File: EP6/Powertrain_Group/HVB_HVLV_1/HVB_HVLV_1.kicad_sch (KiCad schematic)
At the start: 20 parts, among them J1 HV+, J2 HV-, J3 from LV, J5 DCDC-, J6 DCDC+, K1 G7L-2A-X DC24, K2 DBT72410, Q1 IXTH6N100D2, U1 PC817

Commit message: update HVB_HVLV_1 V2.1
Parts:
- removed K1: G7L-2A-X DC24, nturt_kicad_lib_EP6:RELAY_G7L-2A-X_OMR, symbol nturt_kicad_lib_EP6:G7L-2A-X_DC24
- removed K2: DBT72410, DBT72410, symbol SamacSys_Parts_EP6:DBT72410
- added D4, D5, D6, D7: RED LED, LED_SMD:LED_0603_1608Metric, symbol Device:LED
- added J4: DischargeRes-, nturt_kicad_lib_EP6:HRS_DF33C-2P-3.3DSA, symbol Connector_Generic:Conn_01x02
- added J7: DischargeRes+, nturt_kicad_lib_EP6:HRS_DF33C-2P-3.3DSA, symbol Connector_Generic:Conn_01x02
- added K1, K2: G2RG-2A-X DC24, Relay_THT:Relay_DPST_Omron_G2RL-2A, symbol nturt_kicad_lib_EP6:G2RG-2A-X DC24
- added R2, R3, R4, R5: 10k, Resistor_SMD:R_0603_1608Metric, symbol Device:R
- RV1: value 10k -> 10K; footprint PCM_Potentiometer_THT_AKL:Potentiometer_Bourns_3266W_Vertical -> nturt_kicad_lib_EP6:Throughhole Potentiometer 3296W
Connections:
- net +5V: now also D5.2 (A)
- net DCDC_CONTROL: now also D6.2 (A), K1.A2
- net DC_CONTROL: now also D7.2 (A), K2.A1
- net GND: now also K1.A1, K2.A2, R2.2, R3.2, R4.2, R5.2
- net HV+: now also K1.13, K2.24
- net HV-: now also K1.24, K2.13
- net HVpresent: now also D4.2 (A)
- net at J5.1 (Pin_1), J5.2 (Pin_2): now also K1.23
- net at Q1.1 (G), RV1.2, U1.1: now also RV1.3; no longer RV1.1
- net at Q1.3 (S): now also RV1.1; no longer RV1.3
- net at F3.2: now also K1.14
- new net: J4.1 (Pin_1), J4.2 (Pin_2), K2.14
- new net: J7.1 (Pin_1), J7.2 (Pin_2), K2.23
- new net: D5.1 (K), R3.1
- new net: D7.1 (K), R5.1
- new net: D4.1 (K), R2.1
- new net: D6.1 (K), R4.1
- no-connect marks 2 -> 0
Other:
- moved on the sheet: D2, F3, J3, J5, J6

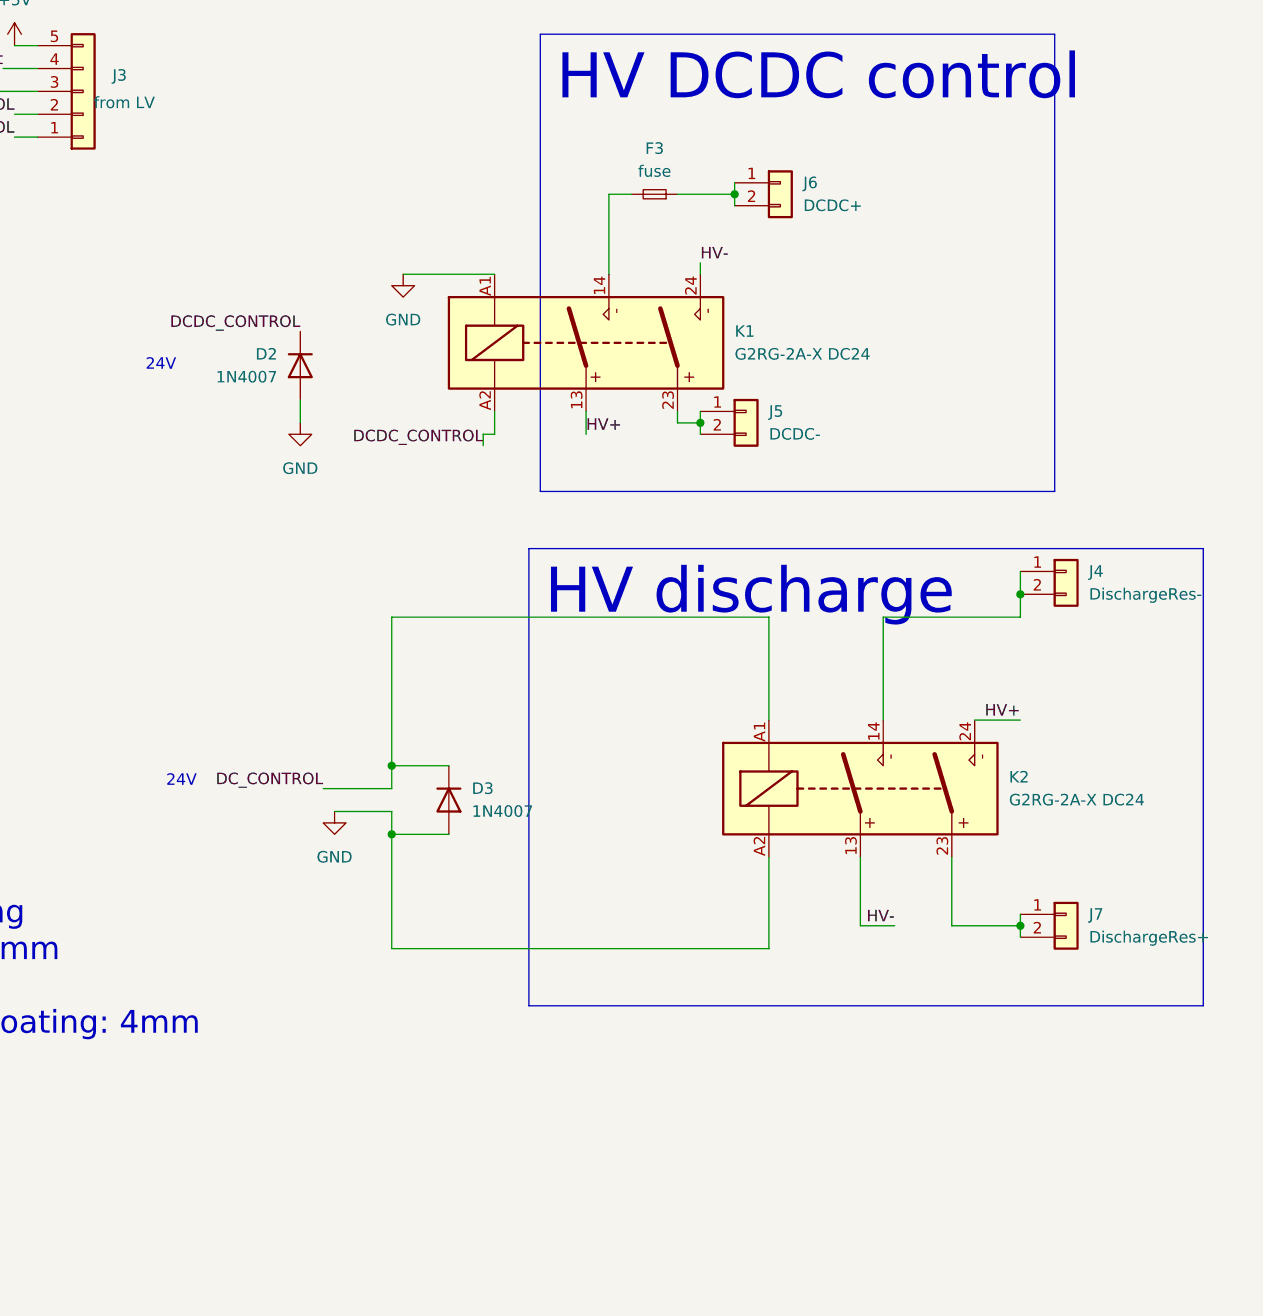
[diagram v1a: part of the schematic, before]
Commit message: update HVB_HVLV_1 to V2.2
V2.2 remove discharge relay
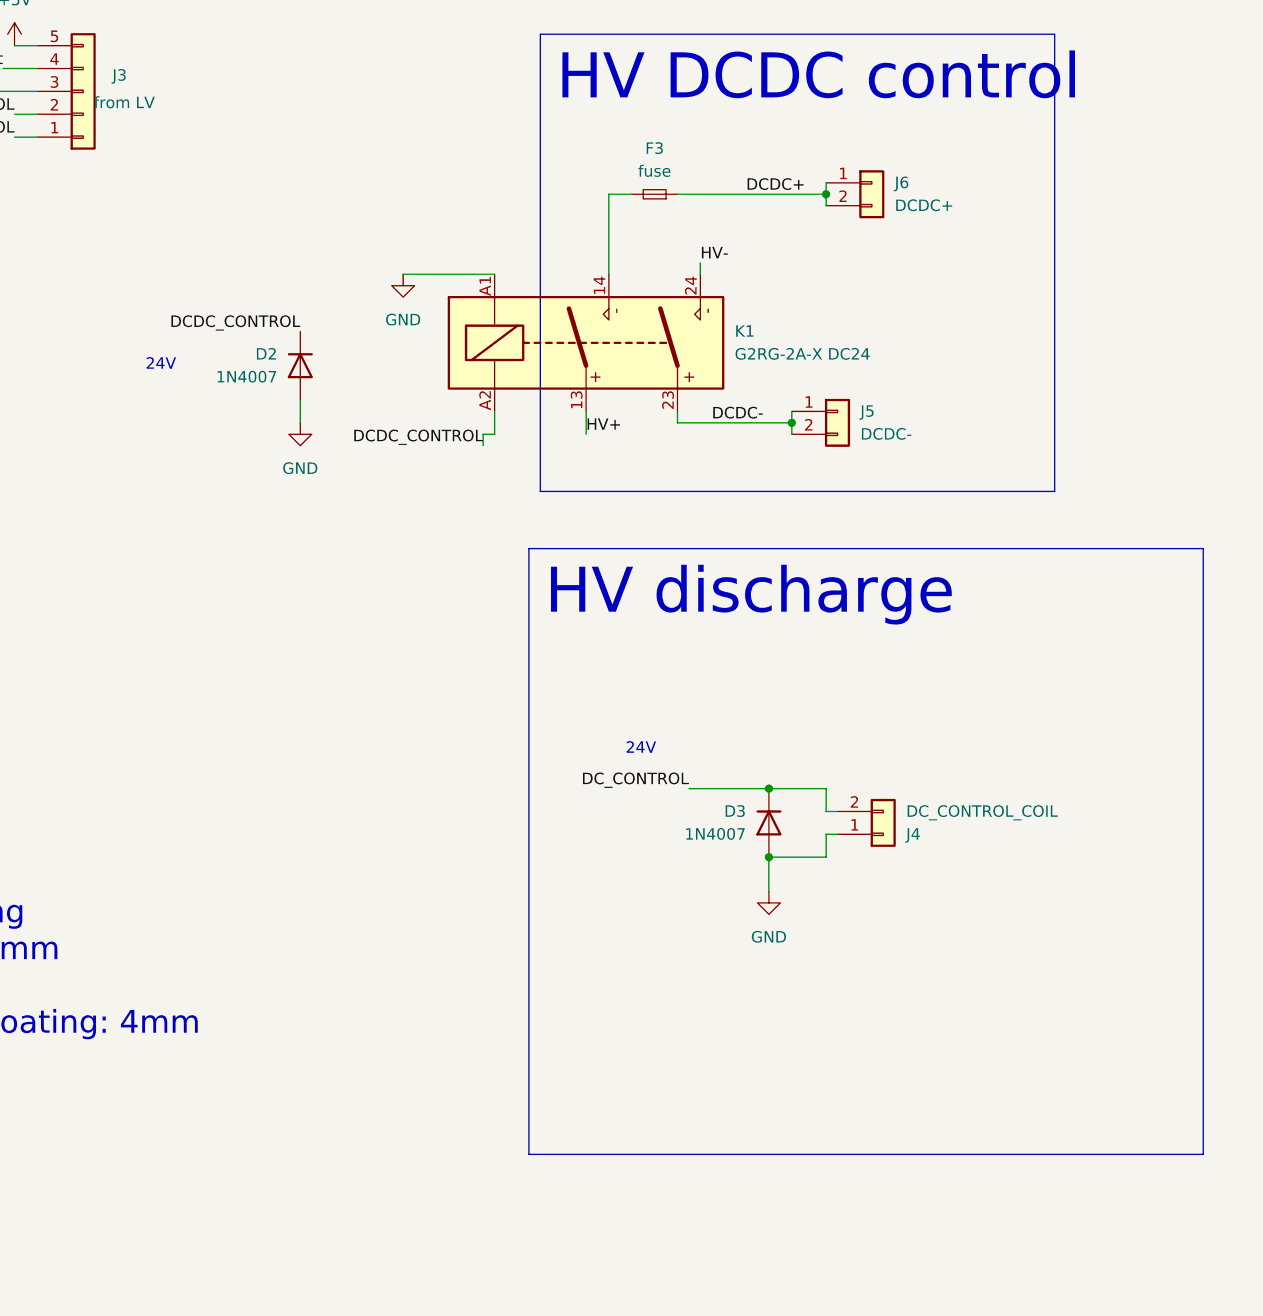
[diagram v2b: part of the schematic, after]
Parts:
- removed J7: DischargeRes+, nturt_kicad_lib_EP6:HRS_DF33C-2P-3.3DSA, symbol Connector_Generic:Conn_01x02
- removed K2: G2RG-2A-X DC24, Relay_THT:Relay_DPST_Omron_G2RL-2A, symbol nturt_kicad_lib_EP6:G2RG-2A-X DC24
- J3: footprint Connector_JST:JST_XH_B5B-XH-A_1x05_P2.50mm_Vertical -> Connector_JST:JST_PH_B5B-PH-K_1x05_P2.00mm_Vertical
- J4: value DischargeRes- -> DC_CONTROL_COIL; footprint nturt_kicad_lib_EP6:HRS_DF33C-2P-3.3DSA -> Connector_JST:JST_VH_B2P-VH_1x02_P3.96mm_Vertical
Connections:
- net DC_CONTROL: now also J4.2 (Pin_2)
- net GND: now also J4.1 (Pin_1)
- net DCDC-: now reaches J5.1 (Pin_1), J5.2 (Pin_2), K1.23
- net DCDC+: now reaches F3.1, J6.1 (Pin_1), J6.2 (Pin_2)
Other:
- moved on the sheet: J5, J6
